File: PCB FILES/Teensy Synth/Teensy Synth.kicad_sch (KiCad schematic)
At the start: 132 parts, among them J1 Conn_01x05, J2 Conn_01x11_Socket, J2 USB_BOOT, J3 RST, J4 Conn_01x04, SW1 SW_Push, SW10 SW_Push, SW11 SW_Push, SW12 SW_Push, SW13 SW_Push, SW14 SW_Push, SW15 SW_Push, SW16 SW_Push, SW17 SW_Push, SW18 SW_Push, SW19 SW_Push, SW2 SW_Push, SW20 SW_Push, SW21 SW_Push, SW22 SW_Push, SW23 SW_Push, SW24 SW_Push, SW25 SW_Push, SW26 SW_Push, SW27 SW_Push, SW28 SW_Push, SW29 SW_Push, SW3 SW_Push, SW30 SW_Push, SW31 SW_Push, SW32 SW_Push, SW33 SW_Push, SW34 SW_Push, SW35 SW_Push, SW36 SW_Push, SW37 SW_Push, SW38 SW_Push, SW39 SW_Push, SW4 SW_Push, SW40 SW_Push, SW41 SW_Push, SW42 SW_Push, SW43 SW_Push, SW44 SW_Push, SW45 SW_Push, SW46 SW_Push, SW47 SW_Push, SW48 RotaryEncoder, SW49 RotaryEncoder, SW5 SW_Push, SW50 RotaryEncoder, SW51 RotaryEncoder, SW52 RotaryEncoder, SW6 SW_Push, SW7 SW_Push, SW8 SW_Push, SW9 SW_Push, U1 RP2040, U1 Teensy4.1, U2 NCP1117-3.3_SOT223, U2 TPS61090, U3 W25Q128JVS, U6 MCP73871, Y1 Crystal_Small

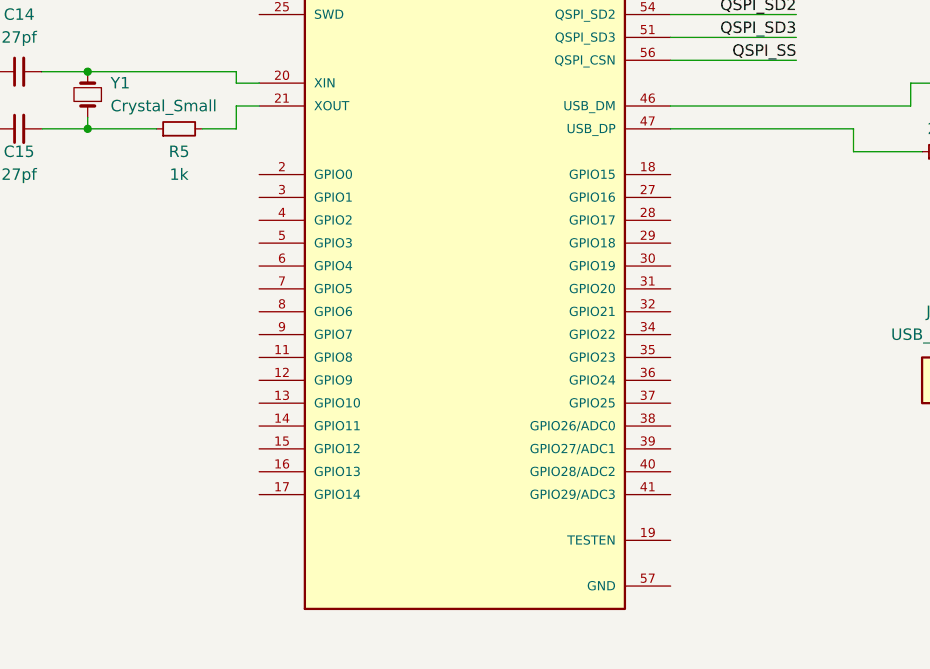
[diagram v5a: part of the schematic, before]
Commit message: Connected the button grid to the RP2040
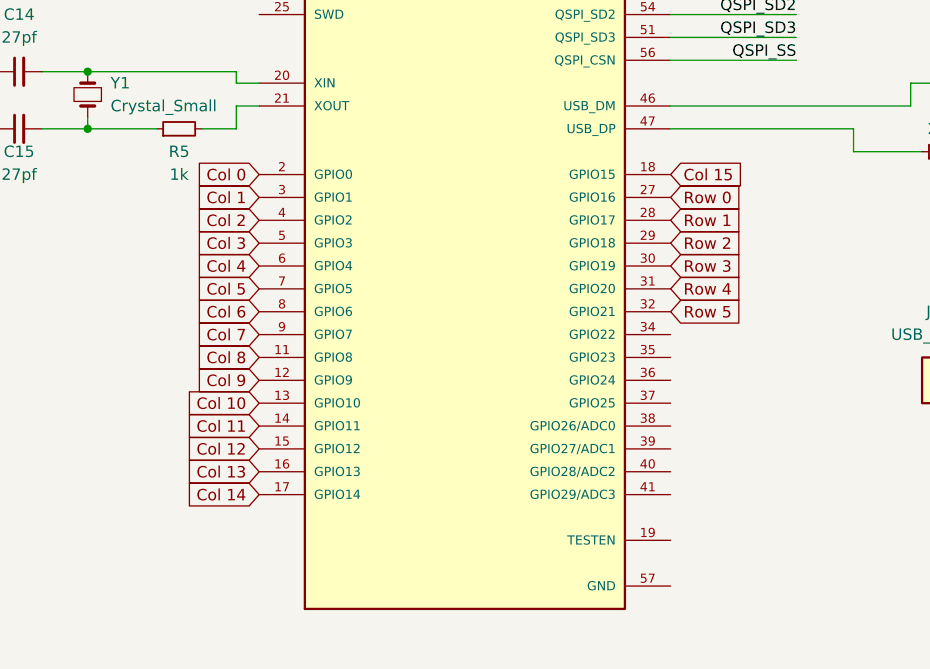
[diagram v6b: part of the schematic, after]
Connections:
- net Col 0: now also U1.2 (GPIO0)
- net Col 1: now also U1.3 (GPIO1)
- net Col 10: now also U1.13 (GPIO10)
- net Col 11: now also U1.14 (GPIO11)
- net Col 12: now also U1.15 (GPIO12)
- net Col 13: now also U1.16 (GPIO13)
- net Col 14: now also U1.17 (GPIO14)
- net Col 15: now also U1.18 (GPIO15)
- net Col 2: now also U1.4 (GPIO2)
- net Col 3: now also U1.5 (GPIO3)
- net Col 4: now also U1.6 (GPIO4)
- net Col 5: now also U1.7 (GPIO5)
- net Col 6: now also U1.8 (GPIO6)
- net Col 7: now also U1.9 (GPIO7)
- net Col 8: now also U1.11 (GPIO8)
- net Col 9: now also U1.12 (GPIO9)
- net Row 0: now also U1.27 (GPIO16)
- net Row 1: now also U1.28 (GPIO17)
- net Row 2: now also U1.29 (GPIO18)
- net Row 3: now also U1.30 (GPIO19)
- net Row 4: now also U1.31 (GPIO20)
- net Row 5: now also U1.32 (GPIO21)
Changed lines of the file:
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@@
+    )
+  )
+  (global_label "Col 9" (shape input) (at 444.5 248.92 180) (fields_autoplaced)
+    (effects (font (size 1.27 1.27)) (justify right))
+    (property "Intersheetrefs" "${INTERSHEET_REFS}" (at 436.2535 248.92 0)
+      (effects (font (size 1.27 1.27)) (justify right) hide)
+    )
+  )
+  (global_label "Col 1" (shape input) (at 444.5 228.6 180) (fields_autoplaced)
+    (effects (font (size 1.27 1.27)) (justify right))
+    (property "Intersheetrefs" "${INTERSHEET_REFS}" (at 436.2535 228.6 0)
+      (effects (font (size 1.27 1.27)) (justify right) hide)
+    )
+  )
+  (global_label "Col 4" (shape input) (at 444.5 236.22 180) (fields_autoplaced)
+    (effects (font (size 1.27 1.27)) (justify right))
+    (property "Intersheetrefs" "${INTERSHEET_REFS}" (at 436.2535 236.22 0)
+      (effects (font (size 1.27 1.27)) (justify right) hide)
     )
   )
@@
     )
   )
+  (global_label "Row 0" (shape input) (at 490.22 228.6 0) (fields_autoplaced)
+    (effects (font (size 1.27 1.27)) (justify left))
+    (property "Intersheetrefs" "${INTERSHEET_REFS}" (at 499.1318 228.6 0)
+      (effects (font (size 1.27 1.27)) (justify left) hide)
+    )
+  )
   (global_label "PWMLight_Screen" (shape input) (at 146.05 64.77 180) (fields_autoplaced)
     (effects (font (size 1.27 1.27)) (justify right))
@@
     )
   )
+  (global_label "Col 10" (shape input) (at 444.5 251.46 180) (fields_autoplaced)
+    (effects (font (size 1.27 1.27)) (justify right))
+    (property "Intersheetrefs" "${INTERSHEET_REFS}" (at 435.044 251.46 0)
+      (effects (font (size 1.27 1.27)) (justify right) hide)
+    )
+  )
   (global_label "Col 3" (shape input) (at 129.54 387.35 270) (fields_autoplaced)
     (effects (font (size 1.27 1.27)) (justify right))
@@
     )
   )
+  (global_label "Row 1" (shape input) (at 490.22 231.14 0) (fields_autoplaced)
+    (effects (font (size 1.27 1.27)) (justify left))
+    (property "Intersheetrefs" "${INTERSHEET_REFS}" (at 499.1318 231.14 0)
+      (effects (font (size 1.27 1.27)) (justify left) hide)
+    )
+  )
+  (global_label "Col 8" (shape input) (at 444.5 246.38 180) (fields_autoplaced)
+    (effects (font (size 1.27 1.27)) (justify right))
+    (property "Intersheetrefs" "${INTERSHEET_REFS}" (at 436.2535 246.38 0)
+      (effects (font (size 1.27 1.27)) (justify right) hide)
+    )
+  )
   (global_label "Enc VA" (shape input) (at 144.78 285.75 270) (fields_autoplaced)
     (effects (font (size 1.27 1.27)) (justify right))
@@
     )
   )
+  (global_label "Col 14" (shape input) (at 444.5 261.62 180) (fields_autoplaced)
+    (effects (font (size 1.27 1.27)) (justify right))
+    (property "Intersheetrefs" "${INTERSHEET_REFS}" (at 435.044 261.62 0)
+      (effects (font (size 1.27 1.27)) (justify right) hide)
+    )
+  )
+  (global_label "Col 15" (shape input) (at 490.22 226.06 0) (fields_autoplaced)
+    (effects (font (size 1.27 1.27)) (justify left))
+    (property "Intersheetrefs" "${INTERSHEET_REFS}" (at 499.676 226.06 0)
+      (effects (font (size 1.27 1.27)) (justify left) hide)
+    )
+  )
   (global_label "Col 6" (shape input) (at 205.74 387.35 270) (fields_autoplaced)
     (effects (font (size 1.27 1.27)) (justify right))
@@
     )
   )
+  (global_label "Col 3" (shape input) (at 444.5 233.68 180) (fields_autoplaced)
+    (effects (font (size 1.27 1.27)) (justify right))
+    (property "Intersheetrefs" "${INTERSHEET_REFS}" (at 436.2535 233.68 0)
+      (effects (font (size 1.27 1.27)) (justify right) hide)
+    )
+  )
   (global_label "Row 2" (shape input) (at 30.48 336.55 180) (fields_autoplaced)
     (effects (font (size 1.27 1.27)) (justify right))
@@
     )
   )
+  (global_label "Row 3" (shape input) (at 490.22 236.22 0) (fields_autoplaced)
+    (effects (font (size 1.27 1.27)) (justify left))
+    (property "Intersheetrefs" "${INTERSHEET_REFS}" (at 499.1318 236.22 0)
+      (effects (font (size 1.27 1.27)) (justify left) hide)
+    )
+  )
+  (global_label "Col 13" (shape input) (at 444.5 259.08 180) (fields_autoplaced)
+    (effects (font (size 1.27 1.27)) (justify right))
+    (property "Intersheetrefs" "${INTERSHEET_REFS}" (at 435.044 259.08 0)
+      (effects (font (size 1.27 1.27)) (justify right) hide)
+    )
+  )
   (global_label "Col 2" (shape input) (at 104.14 387.35 270) (fields_autoplaced)
     (effects (font (size 1.27 1.27)) (justify right))
@@
     )
   )
+  (global_label "Col 0" (shape input) (at 444.5 226.06 180) (fields_autoplaced)
+    (effects (font (size 1.27 1.27)) (justify right))
+    (property "Intersheetrefs" "${INTERSHEET_REFS}" (at 436.2535 226.06 0)
+      (effects (font (size 1.27 1.27)) (justify right) hide)
+    )
+  )
+  (global_label "Col 6" (shape input) (at 444.5 241.3 180) (fields_autoplaced)
+    (effects (font (size 1.27 1.27)) (justify right))
+    (property "Intersheetrefs" "${INTERSHEET_REFS}" (at 436.2535 241.3 0)
+      (effects (font (size 1.27 1.27)) (justify right) hide)
+    )
+  )
   (global_label "I2S Data" (shape input) (at 146.05 78.74 180) (fields_autoplaced)
     (effects (font (size 1.27 1.27)) (justify right))
@@
     )
   )
+  (global_label "Row 2" (shape input) (at 490.22 233.68 0) (fields_autoplaced)
+    (effects (font (size 1.27 1.27)) (justify left))
+    (property "Intersheetrefs" "${INTERSHEET_REFS}" (at 499.1318 233.68 0)
+      (effects (font (size 1.27 1.27)) (justify left) hide)
+    )
+  )
   (global_label "Row 1" (shape input) (at 30.48 323.85 180) (fields_autoplaced)
     (effects (font (size 1.27 1.27)) (justify right))
@@
     )
   )
+  (global_label "Col 2" (shape input) (at 444.5 231.14 180) (fields_autoplaced)
+    (effects (font (size 1.27 1.27)) (justify right))
+    (property "Intersheetrefs" "${INTERSHEET_REFS}" (at 436.2535 231.14 0)
+      (effects (font (size 1.27 1.27)) (justify right) hide)
+    )
+  )
   (global_label "GND" (shape input) (at 241.3 295.91 180) (fields_autoplaced)
     (effects (font (size 1.27 1.27)) (justify right))
@@
     )
   )
+  (global_label "Col 5" (shape input) (at 444.5 238.76 180) (fields_autoplaced)
+    (effects (font (size 1.27 1.27)) (justify right))
+    (property "Intersheetrefs" "${INTERSHEET_REFS}" (at 436.2535 238.76 0)
+      (effects (font (size 1.27 1.27)) (justify right) hide)
+    )
+  )
   (global_label "Enc 1A" (shape input) (at 246.38 285.75 270) (fields_autoplaced)
     (effects (font (size 1.27 1.27)) (justify right))
@@
     )
   )
+  (global_label "Row 5" (shape input) (at 490.22 241.3 0) (fields_autoplaced)
+    (effects (font (size 1.27 1.27)) (justify left))
+    (property "Intersheetrefs" "${INTERSHEET_REFS}" (at 499.1318 241.3 0)
+      (effects (font (size 1.27 1.27)) (justify left) hide)
+    )
+  )
   (global_label "5V" (shape input) (at 146.05 83.82 180) (fields_autoplaced)
     (effects (font (size 1.27 1.27)) (justify right))
@@
     )
   )
+  (global_label "Row 4" (shape input) (at 490.22 238.76 0) (fields_autoplaced)
+    (effects (font (size 1.27 1.27)) (justify left))
+    (property "Intersheetrefs" "${INTERSHEET_REFS}" (at 499.1318 238.76 0)
+      (effects (font (size 1.27 1.27)) (justify left) hide)
+    )
+  )
+  (global_label "Col 11" (shape input) (at 444.5 254 180) (fields_autoplaced)
+    (effects (font (size 1.27 1.27)) (justify right))
+    (property "Intersheetrefs" "${INTERSHEET_REFS}" (at 435.044 254 0)
+      (effects (font (size 1.27 1.27)) (justify right) hide)
+    )
+  )
   (global_label "Col 4" (shape input) (at 154.94 387.35 270) (fields_autoplaced)
     (effects (font (size 1.27 1.27)) (justify right))
@@
     )
   )
+  (global_label "Col 12" (shape input) (at 444.5 256.54 180) (fields_autoplaced)
+    (effects (font (size 1.27 1.27)) (justify right))
+    (property "Intersheetrefs" "${INTERSHEET_REFS}" (at 435.044 256.54 0)
+      (effects (font (size 1.27 1.27)) (justify right) hide)
+    )
+  )
   (global_label "D+" (shape input) (at 523.24 223.52 0) (fields_autoplaced)
     (effects (font (size 1.27 1.27)) (justify left))
@@
       (effects (font (size 1.27 1.27)) (justify right) hide)
     )
+  )
+  (global_label "Col 7" (shape input) (at 444.5 243.84 180) (fields_autoplaced)
+    (effects (font (size 1.27 1.27)) (justify right))
+    (property "Intersheetrefs" "${INTERSHEET_REFS}" (at 436.2535 243.84 0)
+      (effects (font (size 1.27 1.27)) (justify right) hide)
+    )

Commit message: more hookups
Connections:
- net Col 1: now also SW7.2
- net Col 10: now also SW32.2, SW33.2, SW34.2; no longer SW29.2, SW30.2, SW31.2
- net Col 11: now also SW35.2, SW36.2, SW37.2; no longer SW32.2, SW33.2, SW34.2
- net Col 12: now also SW38.2, SW39.2; no longer SW35.2, SW36.2, SW37.2
- net Col 13: now also SW40.2, SW41.2, SW42.2; no longer SW38.2, SW39.2
- net Col 14: now also SW43.2, SW44.2, SW45.2, SW46.2, SW47.2; no longer SW40.2, SW41.2, SW42.2
- net Col 2: now also SW10.2, SW11.2, SW12.2, SW8.2, SW9.2; no longer SW7.2
- net Col 3: now also SW13.2, SW14.2, SW15.2; no longer SW10.2, SW11.2, SW12.2, SW8.2, SW9.2
- net Col 4: now also SW16.2, SW17.2, SW18.2; no longer SW13.2, SW14.2, SW15.2
- net Col 5: now also SW19.2, SW20.2; no longer SW16.2, SW17.2, SW18.2
- net Col 6: now also SW21.2, SW22.2, SW23.2; no longer SW19.2, SW20.2
- net Col 7: now also SW24.2, SW25.2, SW26.2; no longer SW21.2, SW22.2, SW23.2
- net Col 8: now also SW27.2, SW28.2; no longer SW24.2, SW25.2, SW26.2
- net Col 9: now also SW29.2, SW30.2, SW31.2; no longer SW27.2, SW28.2
- net Enc 1A: now also U1.34 (GPIO22)
- net Enc 1B: now also U1.35 (GPIO23)
- net Enc 2A: now also U1.36 (GPIO24)
- net Enc 2B: now also U1.37 (GPIO25)
- net Enc 3A: now also U1.38 (GPIO26/ADC0)
- net Enc 3B: now also U1.39 (GPIO27/ADC1)
- net Enc 4A: now also U1.40 (GPIO28/ADC2)
- net Enc 4B: now also U1.41 (GPIO29/ADC3)
- net Row 0: now also U1.18 (GPIO15); no longer U1.27 (GPIO16)
- net Row 1: now also D1.1 (K), D4.1 (K), U1.27 (GPIO16); no longer U1.28 (GPIO17)
- net Row 2: now also D2.1 (K), D5.1 (K), U1.28 (GPIO17); no longer U1.29 (GPIO18)
- net Row 3: now also D3.1 (K), D6.1 (K), U1.29 (GPIO18); no longer D1.1 (K), D4.1 (K), U1.30 (GPIO19)
- net Row 4: now also D12.1 (K), D15.1 (K), D18.1 (K), D20.1 (K), D23.1 (K), D26.1 (K), D28.1 (K), D31.1 (K), D34.1 (K), D37.1 (K), D39.1 (K), D42.1 (K), D47.1 (K), D7.1 (K), U1.30 (GPIO19); no longer D2.1 (K), D5.1 (K), U1.31 (GPIO20)
- removed net Col 15: SW43.2, SW44.2, SW45.2, SW46.2, SW47.2, U1.18 (GPIO15)
- removed net Row 5: D12.1 (K), D15.1 (K), D18.1 (K), D20.1 (K), D23.1 (K), D26.1 (K), D28.1 (K), D3.1 (K), D31.1 (K), D34.1 (K), D37.1 (K), D39.1 (K), D42.1 (K), D47.1 (K), D6.1 (K), D7.1 (K), U1.32 (GPIO21)
- new net SCL: U1.32 (GPIO21)
- new net SDA: U1.31 (GPIO20)

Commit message: VAL PLS CONNECT AND COMMIT
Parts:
- removed J1: Conn_01x05, symbol Connector_Generic:Conn_01x05
- added J1: Conn_01x09, Connector_JST:JST_SH_SM09B-SRSS-TB_1x09-1MP_P1.00mm_Horizontal, symbol Connector_Generic:Conn_01x09
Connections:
- net +5V: now also J1.2 (Pin_2)
- net GND: now also J1.1 (Pin_1)
- net VBUS: now also J1.9 (Pin_9)
- new net I2C_SCL: J1.4 (Pin_4)
- new net I2C_SDA: J1.3 (Pin_3)
- new net I2S Bit Clock: J1.6 (Pin_6)
- new net I2S D In: J1.8 (Pin_8)
- new net I2S D Out: J1.7 (Pin_7)
- new net I2S Frame Clock: J1.5 (Pin_5)
